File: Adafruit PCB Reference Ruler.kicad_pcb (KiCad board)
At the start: 2 copper layers, 101 x 25.4 mm, 63 parts

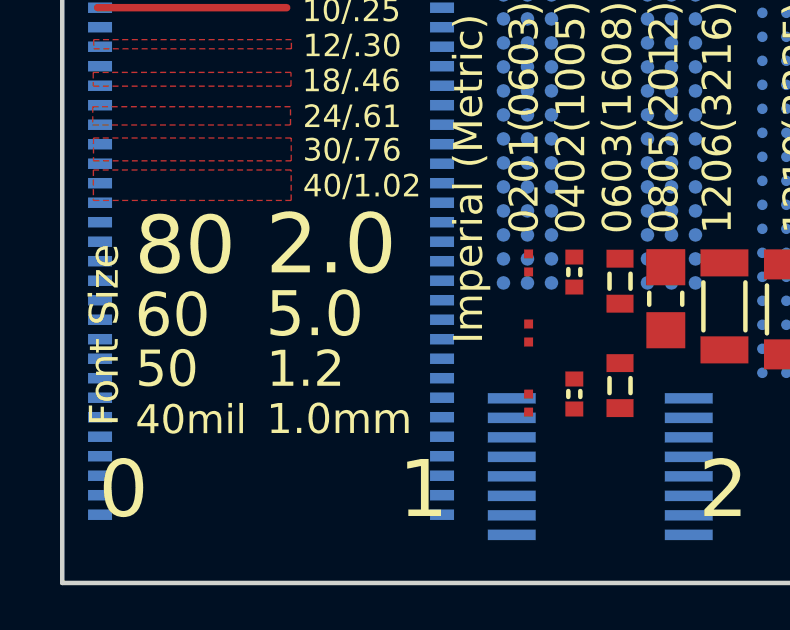
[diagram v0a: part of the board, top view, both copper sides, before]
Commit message: Fixed typos
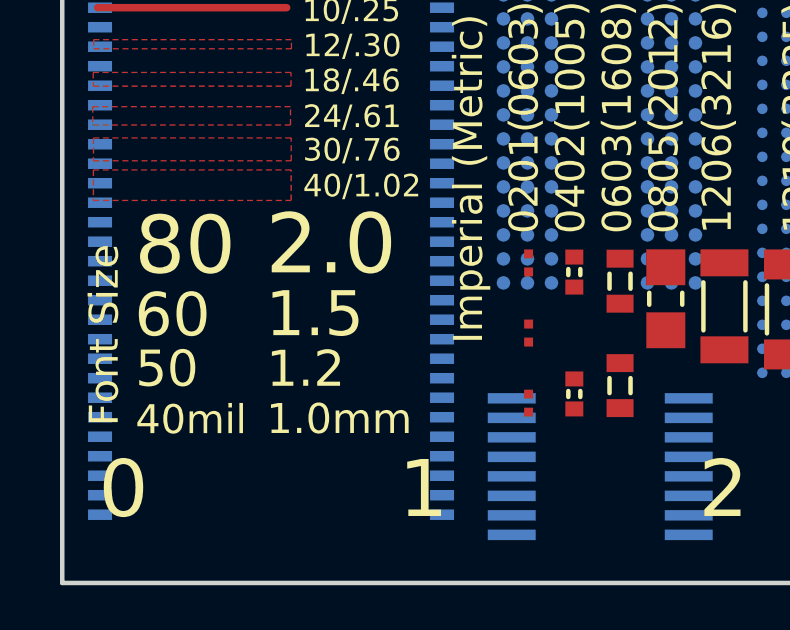
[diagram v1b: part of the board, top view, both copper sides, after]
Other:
- board text added: "1.5"
- board text removed: "5.0"
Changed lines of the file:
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@@
     (effects (font (size 2 2) (thickness 0.2)) (justify left bottom))
   )
-  (gr_text 5.0 (at 77.8129 109.6264) (layer F.SilkS)
+  (gr_text 1.5 (at 77.8129 109.6264) (layer F.SilkS)
     (effects (font (size 1.5 1.5) (thickness 0.15)) (justify left bottom))
   )
